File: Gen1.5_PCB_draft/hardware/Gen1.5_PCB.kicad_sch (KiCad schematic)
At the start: 10 parts, among them J1 Enc1, J12 Enc2, J13 Enc3, J14 Enc4, J2 IMU, J3 Booster, J5 Roboclaw1, J6 Roboclaw2, J7 Roboclaw3, U1 ESP32-P4-ETH

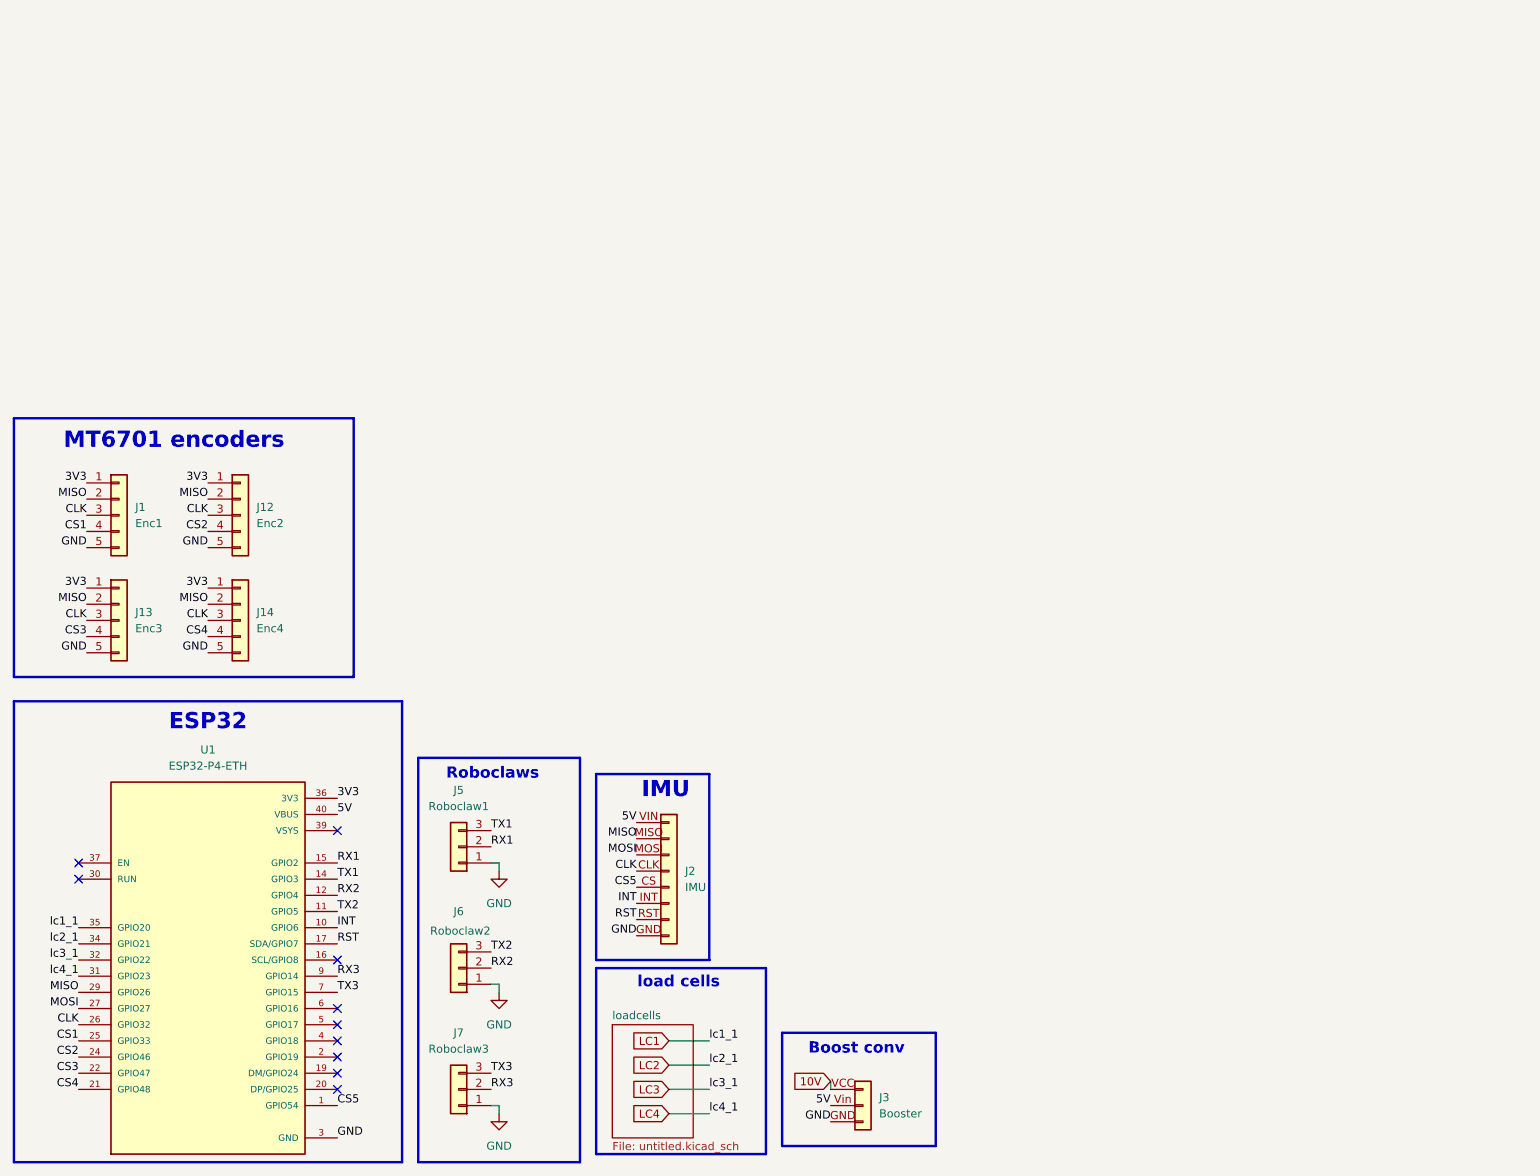
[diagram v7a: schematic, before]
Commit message: added can circuit back into gen1.5 board
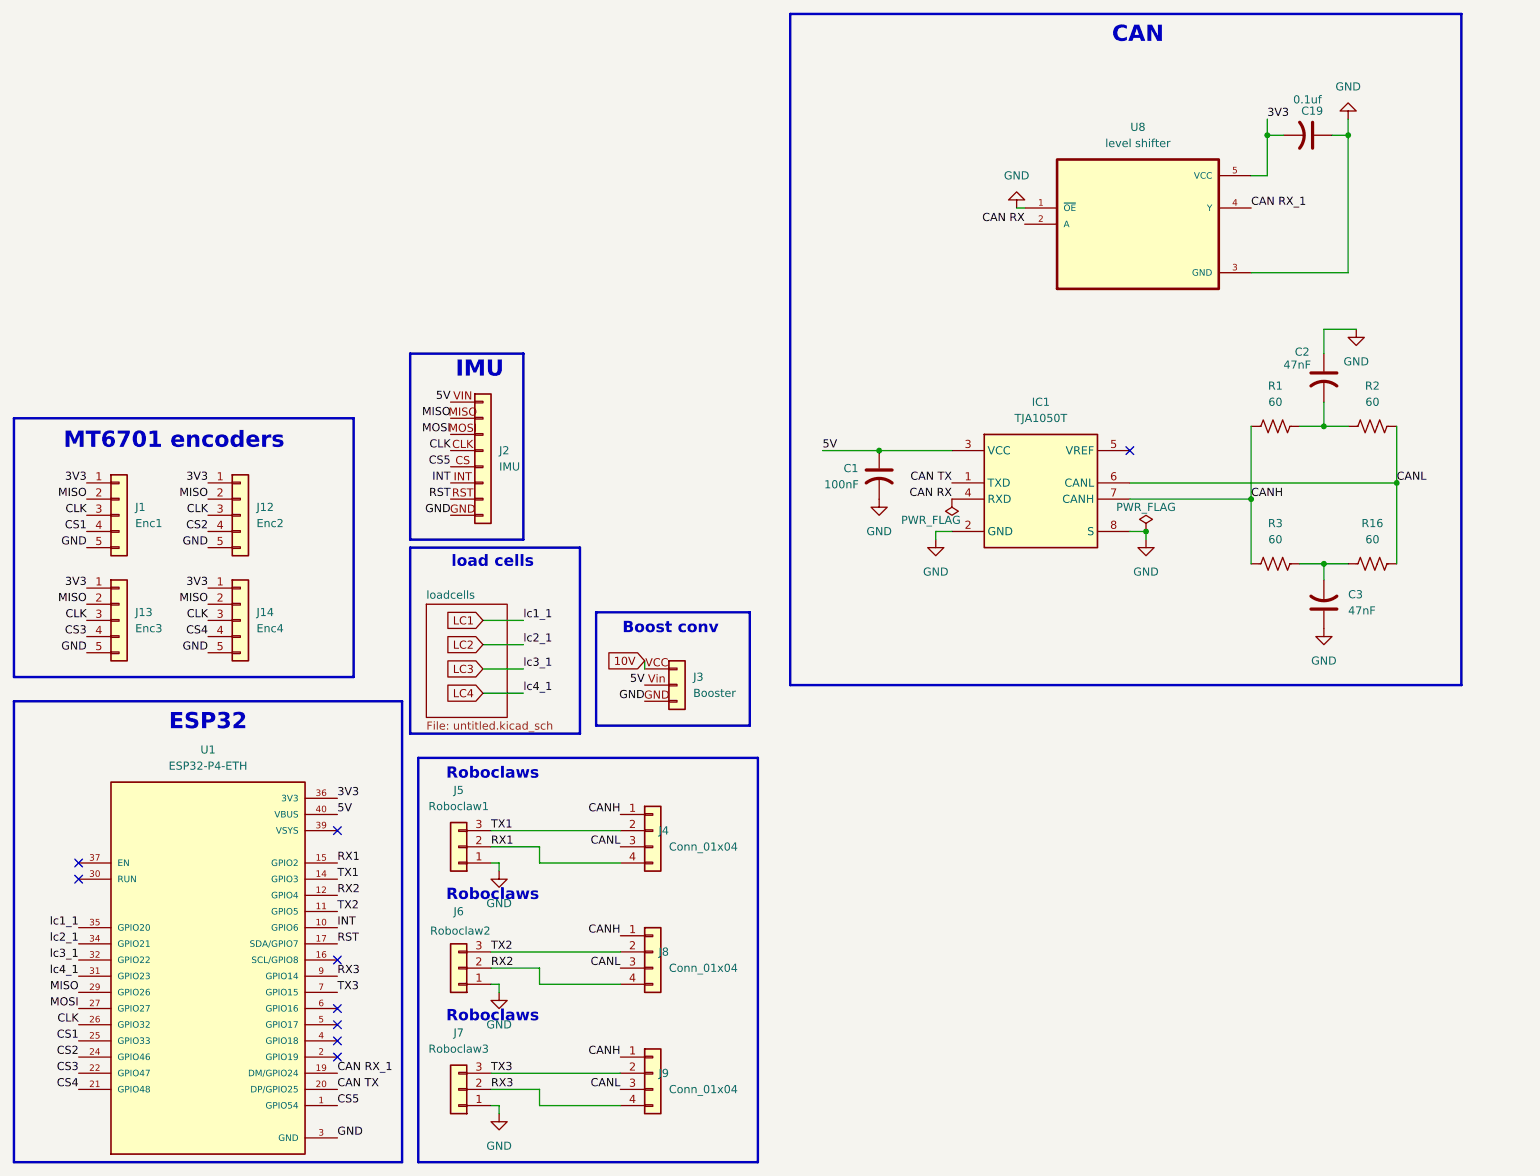
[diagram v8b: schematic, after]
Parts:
- added C1: 100nF, CAN_test_board:CAPC2012X145N, symbol Device:C_US
- added C19: 0.1uf, CAN_test_board:CAPC2012X145N, symbol Device:C_US
- added C2, C3: 47nF, CAN_test_board:CAPC2012X145N, symbol Device:C_US
- added IC1: TJA1050T, CAN_test_board:TJA1050T, symbol Gen1.5_PCB:TJA1050T
- added J4, J8, J9: Conn_01x04, symbol Connector_Generic:Conn_01x04
- added R1, R16, R2, R3: 60, CAN_test_board:RESC3116X65N, symbol Device:R_US
- added U8: level shifter, CAN_test_board:SOT95P280X145-5N, symbol Gen1.5_PCB:SN74LVC1G125DBVR
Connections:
- net 3V3: now also C19.2, U8.5 (VCC)
- net 5V: now also C1.1, IC1.3 (VCC)
- net GND: now also C1.2, C19.1, C2.1, C3.1, IC1.2 (GND), IC1.8 (S), U8.1 (~{OE}), U8.3 (GND)
- net RX1: now also J4.4 (Pin_4)
- net RX2: now also J8.4 (Pin_4)
- net RX3: now also J9.4 (Pin_4)
- net TX1: now also J4.2 (Pin_2)
- net TX2: now also J8.2 (Pin_2)
- net TX3: now also J9.2 (Pin_2)
- net CAN RX_1: now reaches U1.19 (DM/GPIO24)
- net CAN RX_1: now also U8.4 (Y)
- net CAN TX: now reaches U1.20 (DP/GPIO25)
- net CAN TX: now also IC1.1 (TXD)
- new net: C2.2, R1.2, R2.1
- new net: C3.2, R16.1, R3.2
- new net CAN RX: IC1.4 (RXD), U8.2 (A)
- new net CANH: IC1.7 (CANH), J4.1 (Pin_1), J8.1 (Pin_1), J9.1 (Pin_1), R1.1, R3.1
- new net CANL: IC1.6 (CANL), J4.3 (Pin_3), J8.3 (Pin_3), J9.3 (Pin_3), R16.2, R2.2
- no-connect marks 10 -> 9
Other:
- note added: "CAN"
- moved on the sheet: J2, J3
